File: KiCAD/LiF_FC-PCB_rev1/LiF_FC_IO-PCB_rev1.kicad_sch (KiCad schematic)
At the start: 45 parts, among them J1 Left, J2 Right, SW10 TL3301PF160QG, SW11 TL3301PF160QG, SW4 TL3301PF160QG, SW5 TL3301PF160QG, SW6 TL3301PF160QG, SW7 TL3301PF160QG, SW8 TL3301PF160QG, SW9 TL3301PF160QG, U13 DC56-11EWA

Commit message: finished service PCB routing and silkscreen, finished IO PCB layout, routing, and silkscreen. Exported production files, submitted PCB for manufacturing by JLCPCB
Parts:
- removed J1: Left, Connector_PinSocket_2.54mm:PinSocket_1x16_P2.54mm_Vertical, symbol Connector:Conn_01x16_Socket
- removed J2: Right, Connector_PinSocket_2.54mm:PinSocket_1x16_P2.54mm_Vertical, symbol Connector:Conn_01x16_Socket
- added J1: Top, Connector_PinSocket_2.54mm:PinSocket_1x10_P2.54mm_Vertical, symbol Connector:Conn_01x10_Socket
- added J2: Right, Connector_PinSocket_2.54mm:PinSocket_1x19_P2.54mm_Vertical, symbol Connector:Conn_01x19_Socket
- added J3: Left, Connector_PinSocket_2.54mm:PinSocket_1x16_P2.54mm_Vertical, symbol Connector:Conn_01x16_Socket
- renumbered C43 to C1, C55 to C10, C54 to C11, C44 to C2, C45 to C3, C46 to C4, C47 to C5, C50 to C6, C51 to C7, C52 to C8, C56 to C9, D16 to D1, D17 to D2, D18 to D3, D19 to D4, D20 to D5, D21 to D6, D22 to D7, D23 to D8, R61 to R1, R73 to R10, R71 to R11, R62 to R2, R63 to R3, R64 to R4, R65 to R5, R67 to R6, R68 to R7, R69 to R8, R74 to R9, SW4 to SW1, SW5 to SW2, SW6 to SW3, SW7 to SW4, SW8 to SW5, SW9 to SW6, SW10 to SW7, SW11 to SW8, U13 to U1
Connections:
- net ENC_3V3 is gone; now on net +3.3V: R10.1, R11.1, R9.1
- net DIG1_A: now also RN2.14, U1.16 (DIG1_A); no longer RN1.8
- net DIG1_B: now also RN2.13, U1.15 (DIG1_B); no longer RN1.7
- net DIG1_C: now also RN1.11, U1.3 (DIG1_C); no longer RN1.6
- net DIG1_D: now also RN1.10, U1.2 (DIG1_D); no longer RN1.5
- net DIG1_DP: now also RN1.12, U1.4 (DP1); no longer RN1.1
- net DIG1_E: now also RN1.9, U1.1 (DIG1_E); no longer RN1.4
- net DIG1_F: now also RN2.16, U1.18 (DIG1_F); no longer RN1.3
- net DIG1_G: now also RN2.15, U1.17 (DIG1_G); no longer RN1.2
- net DIG2_A: now also RN2.11, U1.11 (DIG2_A); no longer RN2.8
- net DIG2_B: now also RN2.10, U1.10 (DIG2_B); no longer RN2.7
- net DIG2_C: now also RN1.16, U1.8 (DIG2_C); no longer RN2.6
- net DIG2_D: now also RN1.14, U1.6 (DIG2_D); no longer RN2.5
- net DIG2_DP: now also RN2.9, U1.9 (DP2); no longer RN2.1
- net DIG2_E: now also RN1.13, U1.5 (DIG2_E); no longer RN2.4
- net DIG2_F: now also RN2.12, U1.12 (DIG2_F); no longer RN2.3
- net DIG2_G: now also RN1.15, U1.7 (DIG2_G); no longer RN2.2
- net GND: now also J1.1 (Pin_1), J1.10 (Pin_10), J1.2 (Pin_2), J1.3 (Pin_3)
- net IN8: now reaches C11.1, MT1.2, R11.2
- net IN8: now also J2.9 (Pin_9)
- net IN5: now reaches C6.1, R6.2, SW6.1, SW6.2
- net IN5: now also J2.6 (Pin_6)
- net IN4: now reaches C5.1, R5.2, SW5.1, SW5.2
- net IN4: now also J2.5 (Pin_5)
- net IN1: now reaches C2.1, R2.2, SW2.1, SW2.2
- net IN1: now also J2.2 (Pin_2)
- net IN3: now reaches C4.1, R4.2, SW4.1, SW4.2
- net IN3: now also J2.4 (Pin_4)
- net IN2: now reaches C3.1, R3.2, SW3.1, SW3.2
- net IN2: now also J2.3 (Pin_3)
- net IN6: now reaches C7.1, R7.2, SW7.1, SW7.2
- net IN6: now also J2.7 (Pin_7)
- net IN10: now reaches C9.1, MT1.B, R9.2
- net IN10: now also J2.11 (Pin_11)
- net IN0: now reaches C1.1, R1.2, SW1.1, SW1.2
- net IN0: now also J2.1 (Pin_1)
- net IN9: now reaches C10.1, MT1.A, R10.2
- net IN9: now also J2.10 (Pin_10)
- net IN7: now reaches C8.1, R8.2, SW8.1, SW8.2
- net IN7: now also J2.8 (Pin_8)
- net BTN_3V3 renamed +3.3V
- net +3.3V: now also J1.4 (Pin_4), J1.5 (Pin_5)
- net LED0 renamed IO16
- net IO16: now also J2.12 (Pin_12)
- net LED1 renamed IO17
- net IO17: now also J2.13 (Pin_13)
- net LED2 renamed IO18
- net IO18: now also J2.14 (Pin_14)
- net LED3 renamed IO19
- net IO19: now also J2.15 (Pin_15)
- net LED4 renamed IO20
- net IO20: now also J2.16 (Pin_16)
- net LED5 renamed IO21
- net IO21: now also J2.17 (Pin_17)
- net LED6 renamed IO22
- net IO22: now also J2.18 (Pin_18)
- net LED7 renamed IO23
- net IO23: now also J2.19 (Pin_19)
- new net +5V: J1.6 (Pin_6), J1.7 (Pin_7)
- new net IO0: J3.1 (Pin_1), RN1.8
- new net IO1: J3.2 (Pin_2), RN1.7
- new net IO10: J3.11 (Pin_11), RN2.6
- new net IO11: J3.12 (Pin_12), RN2.5
- new net IO12: J3.13 (Pin_13), RN2.4
- new net IO13: J3.14 (Pin_14), RN2.3
- new net IO14: J3.15 (Pin_15), RN2.2
- new net IO15: J3.16 (Pin_16), RN2.1
- new net IO2: J3.3 (Pin_3), RN1.6
- new net IO3: J3.4 (Pin_4), RN1.5
- new net IO4: J3.5 (Pin_5), RN1.4
- new net IO5: J3.6 (Pin_6), RN1.3
- new net IO6: J3.7 (Pin_7), RN1.2
- new net IO7: J3.8 (Pin_8), RN1.1
- new net IO8: J3.9 (Pin_9), RN2.8
- new net IO9: J3.10 (Pin_10), RN2.7
- new net VS: J1.8 (Pin_8), J1.9 (Pin_9)
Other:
- note removed: "Debounce"
- note removed: "Floor 2"
- note removed: "Function (car controller) Encoder will be rotated and the value will be updated on the 7-seg display. This will behave as a floor selector Delete if not wanted :("
- note removed: "Pull up R's for input"
- moved on the sheet: C1, C10, C11, C2, C3, C4, C5, C6, C7, C8, C9, MT1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

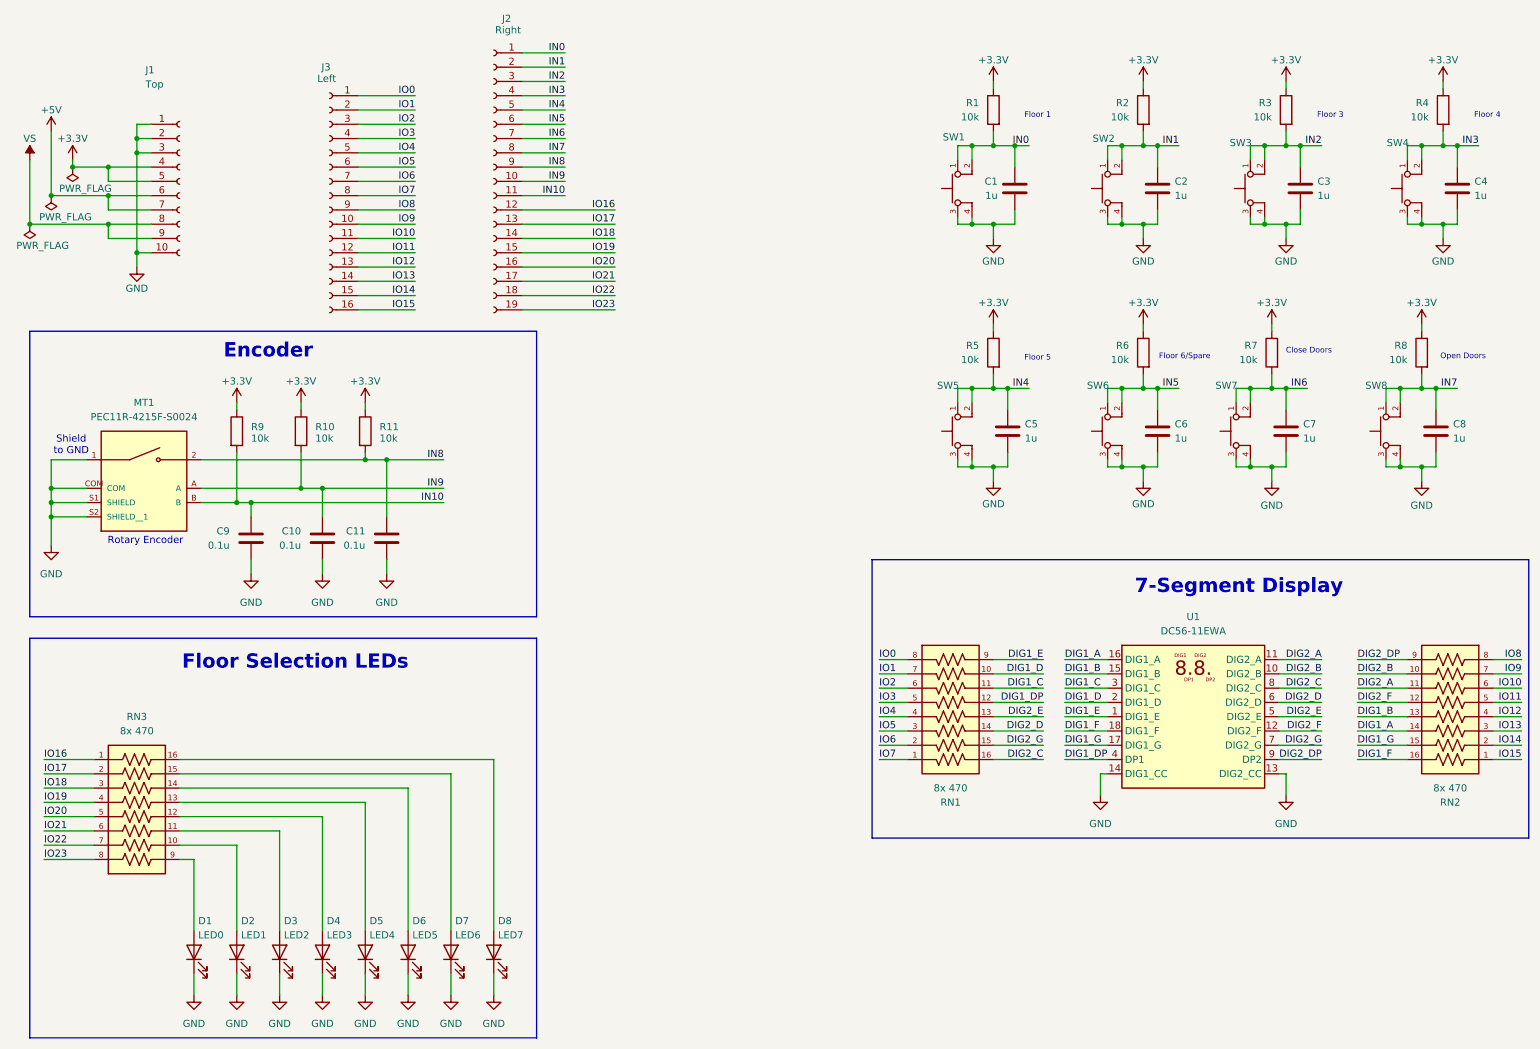
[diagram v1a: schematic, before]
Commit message: touched up IO schematics and exported schematics PDF
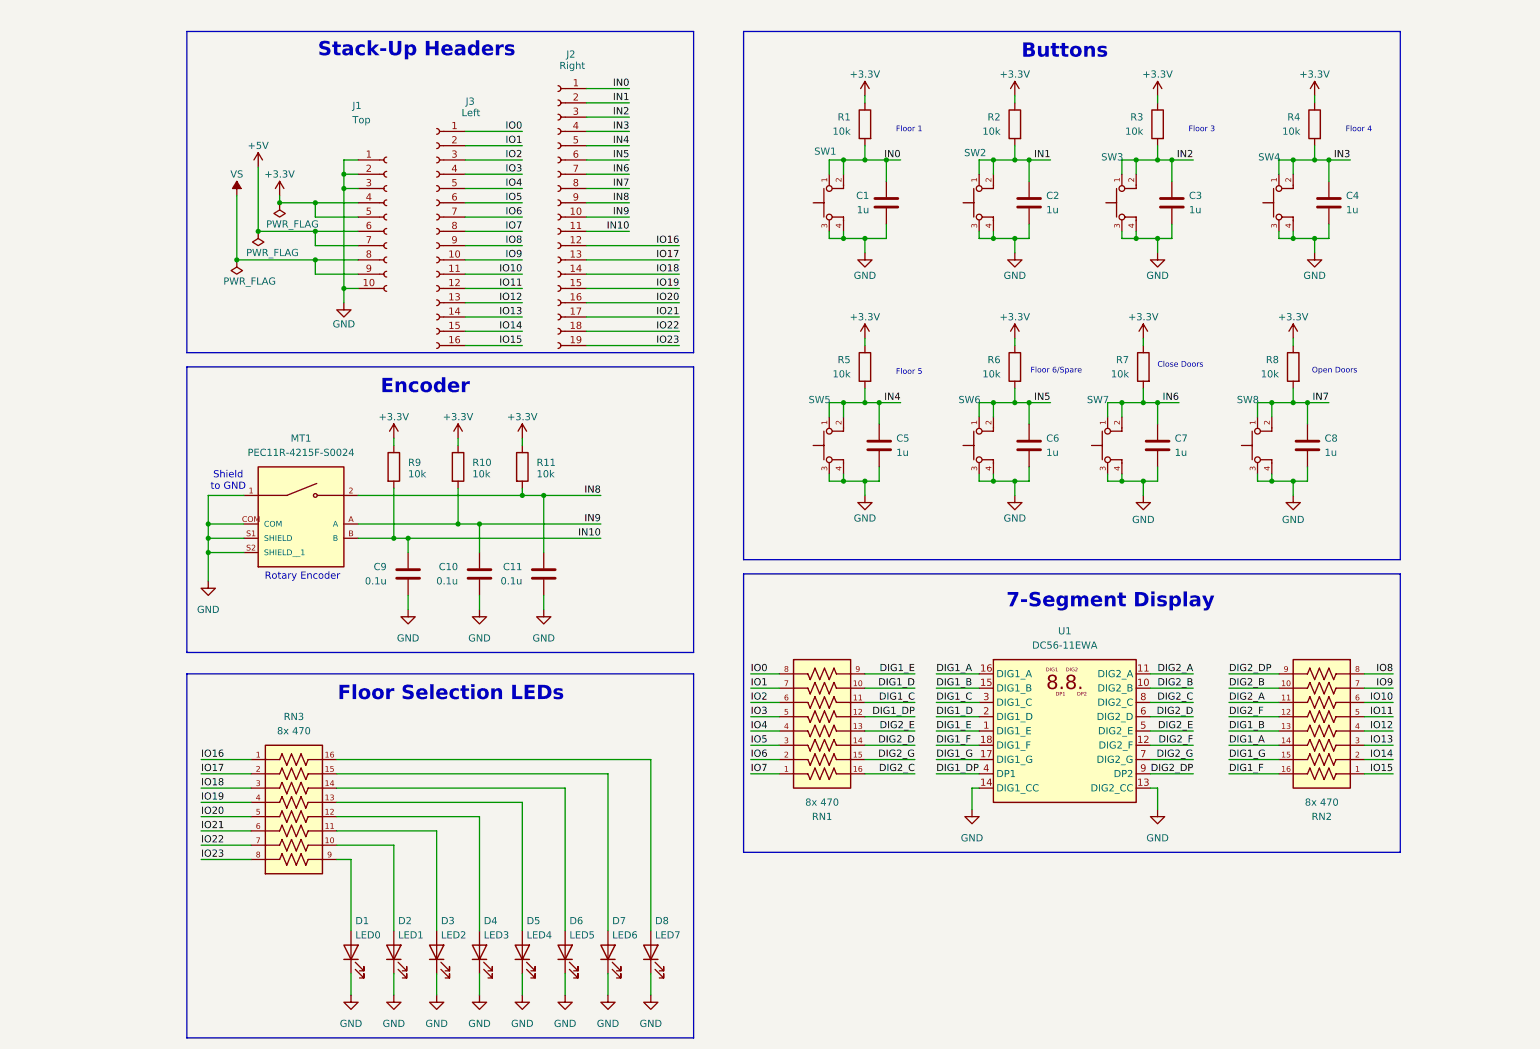
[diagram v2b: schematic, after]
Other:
- note added: "Buttons"
- note added: "Stack-Up Headers"
- company: (none) -> Designed by MR, NK
- title: (none) -> Lithium Firefly FC I/O
- moved on the sheet: C1, C10, C11, C2, C3, C4, C5, C6, C7, C8, C9, D1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
